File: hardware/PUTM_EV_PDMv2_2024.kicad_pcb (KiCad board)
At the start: 4 copper layers, 58 x 87.3 mm, 159 parts, among them IC1 BTS722204ESAXUMA1, IC2 BTS722204ESAXUMA1, IC3 BTS722204ESAXUMA1, IC4 BTS722204ESAXUMA1, J1 74650073R, J4 Conn_01x06, J5 UMPT-08-01-L-RA-WT-P-TR, J6 FTSH-107-01-L-DV-K-A, J7 USB_C_Receptacle_USB2.0_14P, J8 UMPT-08-01-L-RA-WT-P-TR, U1 STM32G0C1KCTxN, U2 LD1117S33TR_SOT223, U3 LM2675M-5.0/NOPB, U4 MCP2542FDxMF

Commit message: Changed CAN to isolated and added a new board-to-board plug
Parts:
- removed J4: Conn_01x06, Connector_IDC:IDC-Header_2x03_P2.54mm_Vertical
- removed J5, J8: UMPT-08-01-L-RA-WT-P-TR, UMPT-08-01-L-RA-WT-P-TR:SAMTEC_UMPT-08-01-L-RA-WT-P-TR
- removed the REF** at (174.6, 105.2)
- added C25: 100n, Capacitor_SMD:C_0603_1608Metric_Pad1.08x0.95mm_HandSolder, F.Cu at (211.2, 78.7)
- added C26: 10n, Capacitor_SMD:C_0603_1608Metric_Pad1.08x0.95mm_HandSolder, F.Cu at (211.2, 81.2)
- added C54: 47u, Capacitor_SMD:C_0603_1608Metric_Pad1.08x0.95mm_HandSolder, F.Cu at (211.2, 83.7)
- added C55: 220n, Capacitor_SMD:C_0603_1608Metric_Pad1.08x0.95mm_HandSolder, F.Cu at (211.2, 86.2)
- added C56: 100n, Capacitor_SMD:C_0603_1608Metric_Pad1.08x0.95mm_HandSolder, F.Cu at (211.2, 88.7)
- added C57: 47u, Capacitor_SMD:C_0603_1608Metric_Pad1.08x0.95mm_HandSolder, F.Cu at (211.2, 91.2)
- added C58: 100n, Capacitor_SMD:C_0603_1608Metric_Pad1.08x0.95mm_HandSolder, F.Cu at (211.2, 93.7)
- added C59: 10n, Capacitor_SMD:C_0603_1608Metric_Pad1.08x0.95mm_HandSolder, F.Cu at (211.2, 96.2)
- added D9: 5.3V/400W, Package_TO_SOT_SMD:SOT-23-3, F.Cu at (215.9, 94.1)
- added FB1: 2K@100MHz, Inductor_SMD:L_0805_2012Metric_Pad1.05x1.20mm_HandSolder, F.Cu at (228.7, 78.8)
- added FB2: 2K@100MHz, Inductor_SMD:L_0805_2012Metric_Pad1.05x1.20mm_HandSolder, F.Cu at (228.7, 81.5)
- added FB3: 2K@100MHz, Inductor_SMD:L_0805_2012Metric_Pad1.05x1.20mm_HandSolder, F.Cu at (228.7, 84.3)
- added FB4: 2K@100MHz, Inductor_SMD:L_0805_2012Metric_Pad1.05x1.20mm_HandSolder, F.Cu at (228.7, 87.0)
- added J2: IPBS-110-01-XX-D-GP, IPBS-110-01-T-D-GP:SAMTEC_IPBS-110-01-XX-D-GP, F.Cu at (199.1, 99.3)
- added R66: 100K, Resistor_SMD:R_0603_1608Metric_Pad0.98x0.95mm_HandSolder, F.Cu at (211.2, 98.8)
- added U4: ADM3057ExRW, Package_SO:SOIC-20W_7.5x12.8mm_P1.27mm, F.Cu at (219.8, 84.7)
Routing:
- net CAN_L: track 19.6 -> 10.1 mm
- net CAN_H: track 19.8 -> 10.5 mm
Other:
- board outline removed

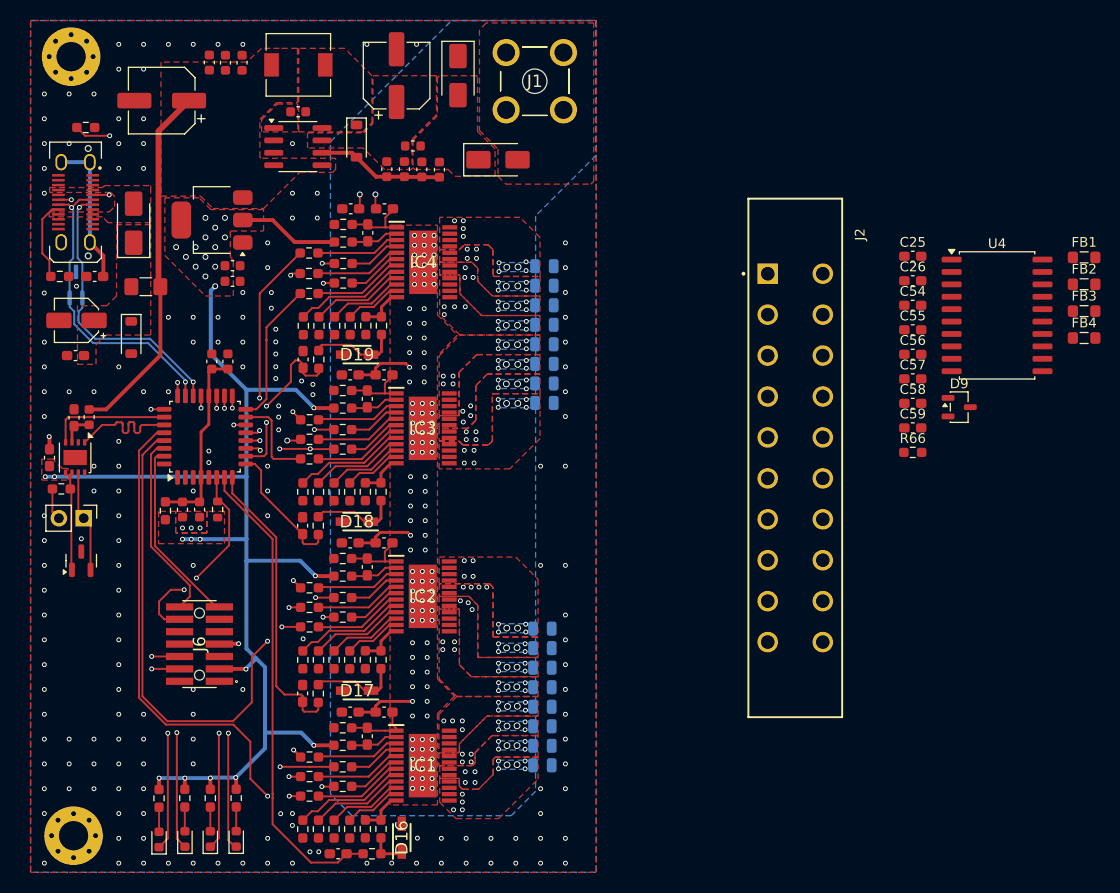
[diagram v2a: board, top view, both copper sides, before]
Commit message: new pcb layout & can coppied from steeringwheel
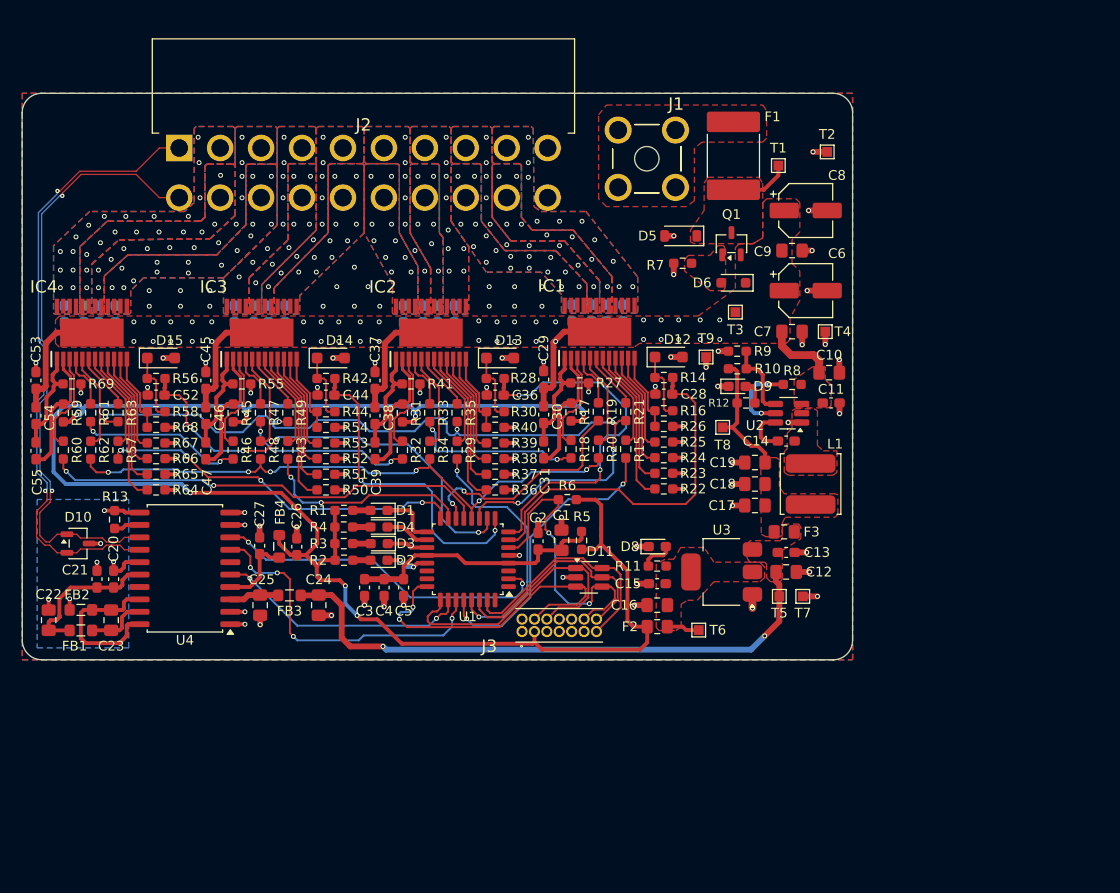
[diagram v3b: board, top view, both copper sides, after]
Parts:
- removed the C25 at (122.8, 99.3)
- removed the C25 at (211.2, 78.7)
- removed the C26 at (125.3, 95.2)
- removed the C26 at (211.2, 81.2)
- removed D16, D17, D18, D19: SKL34, SKL34:SODFL3718X140N
- removed the D9 at (215.9, 94.1)
- removed the D9 at (126.0, 109.8)
- removed the FB2 at (228.7, 81.5)
- removed the FB2 at (126.8, 95.2)
- removed G*** (x2): LOGO, LOGO
- removed G***: LOGO, Logos:SignatureBox25mm
- removed G***: LOGO, logos:PUTM_LOGO_15mm
- removed J6: FTSH-107-01-L-DV-K-A, FTSH-107-01-L-DV-K-A:FTSH-107-XX-YYY-DV-K-A
- removed J7: USB_C_Receptacle_USB2.0_14P, Connector_USB:USB_C_Receptacle_JAE_DX07S024WJ3R400
- removed JP1: Jumper_2_Bridged, Connector_PinHeader_2.54mm:PinHeader_1x02_P2.54mm_Vertical
- removed L2: 47u, Inductor_SMD:L_6.3x6.3_H3
- removed REF** (x2): MountingHole_3mm_Pad_Via, MountingHole:MountingHole_3mm_Pad_Via
- removed the U4 at (125.4, 99.3)
- removed the U4 at (219.8, 84.7)
- added C25: 47u, Capacitor_SMD:C_0805_2012Metric_Pad1.18x1.45mm_HandSolder, F.Cu at (144.3, 114.4)
- added C26: 100n, Capacitor_SMD:C_0603_1608Metric_Pad1.08x0.95mm_HandSolder, F.Cu at (148.1, 108.4)
- added D13: 40V/3A, Diode_SMD:D_SOD-123F, F.Cu at (168.9, 89.1)
- added D14: 40V/3A, Diode_SMD:D_SOD-123F, F.Cu at (151.6, 89.1)
- added D15: 40V/3A, Diode_SMD:D_SOD-123F, F.Cu at (134.2, 89.1)
- added D9: LED_+5V, LED_SMD:LED_0603_1608Metric_Pad1.05x0.95mm_HandSolder, F.Cu at (193.2, 92.0)
- added F2: 6V/1A, Fuse:Fuse_0805_2012Metric_Pad1.15x1.40mm_HandSolder, F.Cu at (185.0, 116.6)
- added F3: 6V/1A, Fuse:Fuse_0805_2012Metric_Pad1.15x1.40mm_HandSolder, F.Cu at (198.0, 106.9)
- added FB2: 2K@100MHz, Inductor_SMD:L_0805_2012Metric_Pad1.05x1.20mm_HandSolder, F.Cu at (126.0, 114.9)
- added J3: FTSH-107-01-L-D-K, PDM:FTSH-107-XX-YYY-D-K, F.Cu at (171.2, 117.1)
- added Q1: 30V/5A, Package_TO_SOT_SMD:SOT-23-3, F.Cu at (192.6, 77.4)
- added R67: 10k, Resistor_SMD:R_0603_1608Metric_Pad0.98x0.95mm_HandSolder, F.Cu at (133.7, 97.8)
- added R68: 1k2, Resistor_SMD:R_0603_1608Metric_Pad0.98x0.95mm_HandSolder, F.Cu at (133.7, 96.2)
- added R69: 47R, Resistor_SMD:R_0603_1608Metric_Pad0.98x0.95mm_HandSolder, F.Cu at (125.1, 91.8)
- added T1: TP_VCC, TestPoint:TestPoint_Pad_1.0x1.0mm, F.Cu at (197.4, 69.4)
- added T2: TP_GND, TestPoint:TestPoint_Pad_1.0x1.0mm, F.Cu at (202.4, 68.0)
- added T3: TP_VCC, TestPoint:TestPoint_Pad_1.0x1.0mm, F.Cu at (193.0, 84.4)
- added T4: TP_GND, TestPoint:TestPoint_Pad_1.0x1.0mm, F.Cu at (202.2, 86.4)
- added T5: TP_+5V, TestPoint:TestPoint_Pad_1.0x1.0mm, F.Cu at (197.5, 113.5)
- added T6: TP_+3V3, TestPoint:TestPoint_Pad_1.0x1.0mm, F.Cu at (189.2, 117.0)
- added T7: TP_GND, TestPoint:TestPoint_Pad_1.0x1.0mm, F.Cu at (199.9, 113.5)
- added T8: TP_+5V, TestPoint:TestPoint_Pad_1.0x1.0mm, F.Cu at (191.7, 96.2)
- added T9: TP_GND, TestPoint:TestPoint_Pad_1.0x1.0mm, F.Cu at (190.0, 89.0)
- added U4: ADM3057ExRW, Package_SO:SOIC-20W_7.5x12.8mm_P1.27mm, F.Cu at (136.7, 110.6)
- C1, C7: value 100n -> 10u; footprint Capacitor_SMD:C_0603_1608Metric -> Capacitor_SMD:C_0805_2012Metric_Pad1.18x1.45mm_HandSolder
- C10, C16: value 100n -> 22u; footprint Capacitor_SMD:C_0603_1608Metric -> Capacitor_SMD:C_0805_2012Metric_Pad1.18x1.45mm_HandSolder
- C11, C15, C5: value 1u -> 100n; footprint Capacitor_SMD:C_0603_1608Metric -> Capacitor_SMD:C_0603_1608Metric_Pad1.08x0.95mm_HandSolder
- C12: value 10n -> 10u; footprint Capacitor_SMD:C_0603_1608Metric -> Capacitor_SMD:C_0805_2012Metric_Pad1.18x1.45mm_HandSolder
- C13: footprint Capacitor_SMD:C_0603_1608Metric -> Capacitor_SMD:C_0603_1608Metric_Pad1.08x0.95mm_HandSolder
- C14: value 68u -> 100n; footprint Capacitor_SMD:CP_Elec_6.3x5.4 -> Capacitor_SMD:C_0603_1608Metric_Pad1.08x0.95mm_HandSolder
- C17: value 220p -> 22u; footprint Capacitor_SMD:C_0603_1608Metric_Pad1.08x0.95mm_HandSolder -> Capacitor_SMD:C_0805_2012Metric_Pad1.18x1.45mm_HandSolder
- C18: value 100n -> 22u; footprint Capacitor_SMD:C_0603_1608Metric_Pad1.08x0.95mm_HandSolder -> Capacitor_SMD:C_0805_2012Metric_Pad1.18x1.45mm_HandSolder
- C19: value 22n -> 22u; footprint Capacitor_SMD:C_0603_1608Metric_Pad1.08x0.95mm_HandSolder -> Capacitor_SMD:C_0805_2012Metric_Pad1.18x1.45mm_HandSolder
- C2: value 4.7u -> 4u7; footprint Capacitor_SMD:C_0603_1608Metric -> Capacitor_SMD:C_0603_1608Metric_Pad1.08x0.95mm_HandSolder
- C20: value 470n -> 100n
- C21: footprint Capacitor_SMD:C_0805_2012Metric -> Capacitor_SMD:C_0603_1608Metric_Pad1.08x0.95mm_HandSolder; moved to F.Cu
- C22, C23, C24: value 10n -> 47u; footprint Capacitor_SMD:C_0805_2012Metric -> Capacitor_SMD:C_0805_2012Metric_Pad1.18x1.45mm_HandSolder; moved to F.Cu
- C27: value 22u -> 10n; footprint Capacitor_SMD:CP_Elec_4x4.5 -> Capacitor_SMD:C_0603_1608Metric_Pad1.08x0.95mm_HandSolder
- C28: value 1u -> 220p
- C29, C37, C45: value 220p -> 100n
- C3: value 100n -> 4u7; footprint Capacitor_SMD:C_0603_1608Metric -> Capacitor_SMD:C_0603_1608Metric_Pad1.08x0.95mm_HandSolder
- C30, C38, C46: value 100n -> 22n
- C31, C39, C47: value 22n -> 470n
- C32, C40, C48: value 470n -> 10n; moved to B.Cu
- C33, C34, C35, C41, C42, C43, C49, C50, C51: footprint Capacitor_SMD:C_0805_2012Metric -> Capacitor_SMD:C_0603_1608Metric_Pad1.08x0.95mm_HandSolder
- C36, C44, C52: value 10n -> 220p; footprint Capacitor_SMD:C_0805_2012Metric -> Capacitor_SMD:C_0603_1608Metric_Pad1.08x0.95mm_HandSolder; moved to F.Cu
- C4: value 4.7u -> 100n; footprint Capacitor_SMD:C_0603_1608Metric -> Capacitor_SMD:C_0603_1608Metric_Pad1.08x0.95mm_HandSolder
- C53: value 10n -> 100n
- C54: value 47u -> 22n
- C55: value 220n -> 470n
- C56, C58: value 100n -> 10n; moved to B.Cu
- C57: value 47u -> 10n; moved to B.Cu
- C59: moved to B.Cu
- C6: value 10u -> 22u; footprint Capacitor_SMD:C_0603_1608Metric -> Capacitor_SMD:CP_Elec_5x5.8
- C8: value 100n -> 22u; footprint Capacitor_SMD:C_0603_1608Metric -> Capacitor_SMD:CP_Elec_5x5.8
- C9: value 100u -> 10u; footprint Capacitor_SMD:CP_Elec_6.3x7.7 -> Capacitor_SMD:C_0805_2012Metric_Pad1.18x1.45mm_HandSolder
- D1, D2, D3, D4: value 150060SS75000 -> LED_Debug; footprint LED_SMD:LED_0603_1608Metric -> LED_SMD:LED_0603_1608Metric_Pad1.05x0.95mm_HandSolder
- D10: value 0.1/1A -> PESD5V0L2BT,215; footprint Diode_SMD:D_SMA -> Package_TO_SOT_SMD:SOT-23-3
- D11: value 6V -> SP0505BAHTG; footprint Diode_SMD:D_SOD-123 -> Package_TO_SOT_SMD:SOT-23-6_Handsoldering
- D12: value TPD2E2U06QDCKRQ1 -> 40V/3A; footprint Package_TO_SOT_SMD:SOT-323_SC-70_Handsoldering -> Diode_SMD:D_SOD-123F; moved to F.Cu
- D5: value SMAJ24CA-13-F -> 30V/200W; footprint Diode_SMD:D_SMA -> Diode_SMD:D_SOD-123
- D6: value SS26FL -> 9V1/200mW; footprint Diode_SMD:D_SOD-123 -> Diode_SMD:D_SOD-323_HandSoldering
- D8: value SS34ALH -> LED_+3V3; footprint Diode_SMD:D_SMA -> LED_SMD:LED_0603_1608Metric_Pad1.05x0.95mm_HandSolder
- F1: value 5V/0.5A -> 33V/1A5; footprint Fuse:Fuse_1206_3216Metric_Pad1.42x1.75mm_HandSolder -> Fuse:Fuse_2920_7451Metric_Pad2.10x5.45mm_HandSolder
- IC1, IC2, IC3, IC4: footprint BTS722204ESAXUMA1:SOP65P600X115-25N -> PDM:SOP65P600X115-25N
- J1: footprint Redcube conn:74650073R -> PDM:74650073R
- J2: footprint IPBS-110-01-T-D-GP:SAMTEC_IPBS-110-01-XX-D-GP -> PDM:IPBT110H1TDRAGP
- L1: value 300n -> 68u/1A4; footprint Inductor_SMD:L_0603_1608Metric -> Inductor_SMD:L_TDK_VLS6045EX_VLS6045AF
- R1, R2, R3, R4: value 150 -> 150R
- R10: value 10k -> 100k
- R11, R12: value 10k -> 1k
- R13: value 1.2k -> 100k
- R14: value 47 -> 4k7
- R15, R16: value 330 -> 4k7
- R17: value 330 -> 470R
- R18, R34, R35, R48, R49, R62, R63: value 330 -> 330R
- R19: value 100k -> 330R; footprint Resistor_SMD:R_0603_1608Metric -> Resistor_SMD:R_0603_1608Metric_Pad0.98x0.95mm_HandSolder
- R20: value 0 -> 330R
- R21: value 120 -> 330R
- R22, R23: value 5.1k -> 10k
- R24, R25, R38, R39, R52, R53: value 4.7k -> 10k
- R26, R40, R54: value 470 -> 1k2
- R27, R41, R55: value 4.7k -> 47R
- R28, R29, R30, R42, R43, R44, R56, R57, R58: value 10k -> 4k7
- R31, R45, R59: value 10k -> 470R
- R32, R46, R60: value 1.2k -> 330R
- R33, R47, R61: value 47 -> 330R
- R36, R37, R50, R51, R64, R65: value 330 -> 10k
- R5: value 4.7k -> 0
- R6: value 4.7k -> 100k
- R66: value 100K -> 10k
- R7: value 470 -> 100k
- R8: value 4.7k -> 510k
- R9: value 10k -> 13k3
- U2: value LD1117S33TR_SOT223 -> TPS54202HDDCR; footprint Package_TO_SOT_SMD:SOT-223-3_TabPin2 -> Package_TO_SOT_SMD:SOT-23-6_Handsoldering
- U3: value LM2675M-5.0/NOPB -> LM1117-3.3; footprint Package_SO:SOIC-8_3.9x4.9mm_P1.27mm -> Package_TO_SOT_SMD:SOT-223-3_TabPin2
- moved FB1 109.6 mm to (126.0, 117.0)
- moved C55 90.6 mm to (121.4, 98.6), turned to -90 degrees
- moved C54 90.5 mm to (121.4, 95.0), turned to -90 degrees
- moved C56 86.9 mm to (124.3, 84.6), turned to -90 degrees
- moved FB3 86.4 mm to (147.3, 113.4)
- moved FB4 85.1 mm to (146.3, 108.4), turned to 90 degrees
- moved C57 85.1 mm to (126.3, 84.6), turned to -90 degrees
- moved C58 83.8 mm to (127.8, 84.6), turned to -90 degrees
- moved C59 82.5 mm to (129.5, 84.6), turned to -90 degrees
- moved R66 77.5 mm to (133.7, 99.4), turned to 180 degrees
- moved C14 72.8 mm to (198.2, 97.6), turned to 0 degrees
- moved C16 72.0 mm to (185.0, 114.4), turned to 180 degrees
- moved J2 70.6 mm to (136.1, 67.6), turned to 0 degrees
- moved R22 69.8 mm to (185.7, 102.5)
- moved C10 69.5 mm to (202.6, 90.6), turned to 0 degrees
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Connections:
- C1 pad 1: /STM_VCC -> /MCU/STM_VCC
- C10 pad 1: +5V -> +24V
- C11 pad 1: +3.3V -> GND
- C11 pad 2: GND -> +24V
- C12 pad 1: /Power/CB -> +5V
- C12 pad 2: /Power/SW_L -> GND
- C13 pad 1: +3.3V -> +5V
- C14 pad 1: +5V -> /Power/BOOT_+5V
- C14 pad 2: GND -> /Power/SW_+5V
- C15 pad 1: +5V -> /Power/VO_+3.3V
- C16 pad 1: +5V -> /Power/VO_+3.3V
- C17 pad 1: /FUSE1_IS -> /Power/+5V_OUT
- C18 pad 1: +BATT -> /Power/+5V_OUT
- C19 pad 1: +BATT -> /Power/+5V_OUT
- C19 pad 2: Net-(IC1-GND_1) -> GND
- C2 pad 1: /STM_VCC -> /MCU/STM_VCC
- C20 pad 1: Net-(IC1-GND_1) -> /CAN/CAN_GND_ISO
- C20 pad 2: Net-(IC1-VDD) -> /CAN/VISOIN
- C21 pad 1: OUT1_0 -> /CAN/VISOIN
- C21 pad 2: GND -> /CAN/CAN_GND_ISO
- C22 pad 1: OUT1_1 -> /CAN/CAN_GND_ISO
- C22 pad 2: GND -> /CAN/VISOIN
- C23 pad 1: OUT1_2 -> /CAN/GNDISO
- C23 pad 2: GND -> /CAN/VISOOUT
- C24 pad 1: OUT1_3 -> GND
- C24 pad 2: GND -> +5V
- C27 pad 1: Net-(D10-K) -> /CAN/VIO
- C28 pad 1: Net-(D10-K) -> /MCU/FUSE_IS0
- C29 pad 1: /FUSE2_IS -> +24V
- C3 pad 1: /STM_VCC -> /MCU/STM_VCC
- C30 pad 1: +BATT -> +24V
- C30 pad 2: GND -> /Power controllers/IC_0/PC0_GND
- C31 pad 1: +BATT -> /Power controllers/IC_0/PC0_GND
- C31 pad 2: Net-(IC2-GND_1) -> /Power controllers/IC_0/VDD
- C32 pad 1: Net-(IC2-GND_1) -> OUT0_0
- C32 pad 2: Net-(IC2-VDD) -> GND
- C33 pad 1: OUT2_0 -> OUT0_1
- C34 pad 1: OUT2_1 -> OUT0_2
- C35 pad 1: OUT2_2 -> OUT0_3
- C36 pad 1: OUT2_3 -> /MCU/FUSE_IS1
- C37 pad 1: /FUSE3_IS -> +24V
- C38 pad 1: +BATT -> +24V
- C38 pad 2: GND -> /Power controllers/IC_1/PC1_GND
- C39 pad 1: +BATT -> /Power controllers/IC_1/PC1_GND
- C39 pad 2: Net-(IC3-GND_1) -> /Power controllers/IC_1/VDD
- C4 pad 1: /STM_VCC -> /MCU/STM_VCC
- C40 pad 1: Net-(IC3-GND_1) -> OUT1_0
- C40 pad 2: Net-(IC3-VDD) -> GND
- C41 pad 1: OUT3_0 -> OUT1_1
- C42 pad 1: OUT3_1 -> OUT1_2
- C43 pad 1: OUT3_2 -> OUT1_3
- C44 pad 1: OUT3_3 -> /MCU/FUSE_IS2
- C45 pad 1: /FUSE4_IS -> +24V
- C46 pad 1: +BATT -> +24V
- C46 pad 2: GND -> /Power controllers/IC_2/PC2_GND
- C47 pad 1: +BATT -> /Power controllers/IC_2/PC2_GND
- C47 pad 2: Net-(IC4-GND_1) -> /Power controllers/IC_2/VDD
- C48 pad 1: Net-(IC4-GND_1) -> OUT2_0
- C48 pad 2: Net-(IC4-VDD) -> GND
- C49 pad 1: OUT4_0 -> OUT2_1
- C5 pad 1: GND -> /MCU/STM_VCC
- C5 pad 2: /Power/VIN_L -> GND
- C50 pad 1: OUT4_1 -> OUT2_2
- C51 pad 1: OUT4_2 -> OUT2_3
- C52 pad 1: OUT4_3 -> /MCU/FUSE_IS3
- C53 pad 1: Net-(J7-SHIELD) -> +24V
- C54 pad 1: /CAN/GNDISO_CAN -> +24V
- C54 pad 2: Net-(U4-VISOIN) -> /Power controllers/IC_3/PC3_GND
- C55 pad 1: Net-(C55-Pad1) -> /Power controllers/IC_3/PC3_GND
- C55 pad 2: Net-(U4-VISOOUT) -> /Power controllers/IC_3/VDD
- C56 pad 1: GND -> OUT3_0
- C56 pad 2: +5V -> GND
- C57 pad 1: GND -> OUT3_1
- C57 pad 2: Net-(U4-VCC) -> GND
- C58 pad 1: +3.3V -> OUT3_2
- C59 pad 1: Net-(U4-VIO) -> OUT3_3
- C6 pad 1: GND -> +24V
- C6 pad 2: /Power/VIN_L -> GND
- C7 pad 1: GND -> +24V
- C7 pad 2: /Power/VIN_SW_REG -> GND
- C8 pad 1: GND -> +24V
- C8 pad 2: /Power/VIN_SW_REG -> GND
- C9 pad 1: /Power/VIN_SW_REG -> +24V
- D1 pad 1: /LED1 -> /MCU/LED3
- D1 pad 2: Net-(D1-A) -> /MCU/LD_3_R
- D10 pad 1: Net-(D10-K) -> /CAN/CAN.N
- D10 pad 2: VBUS -> /CAN/CAN.P
- D11 pad 1: Net-(D10-K) -> /Connectors/SW.CLK
- D12 pad 1: /D- -> /Power controllers/IC_0/R_IS_PROT
- D12 pad 2: /D+ -> GND
- D2 pad 1: /LED2 -> /MCU/LED2
- D2 pad 2: Net-(D2-A) -> /MCU/LD_2_R
- D3 pad 1: /LED3 -> /MCU/LED1
- D3 pad 2: Net-(D3-A) -> /MCU/LD_1_R
- D4 pad 1: /LED4 -> /MCU/LED0
- D4 pad 2: Net-(D4-A) -> /MCU/LD_0_R
- D5 pad 1: GND -> /Power/RPP_D
- D5 pad 2: /Power/VIN_L -> GND
- D6 pad 1: /Power/SW_L -> +24V
- D6 pad 2: GND -> /Power/RPP_G
- D8 pad 1: /Power/VIN_L -> GND
- D8 pad 2: +BATT -> /Power/D3V3_R1k
- F1 pad 1: +5V -> /Power/RPP_D
- F1 pad 2: Net-(D10-K) -> +BATT
- FB1 pad 1: Net-(U4-VISOIN) -> /CAN/VISOIN
- FB1 pad 2: Net-(U4-VISOOUT) -> /CAN/VISOOUT
- FB3 pad 1: Net-(U4-VCC) -> /CAN/VCC
- FB4 pad 1: Net-(U4-VIO) -> /CAN/VIO
- FB4 pad 2: +3.3V -> +3V3
- IC1 pad 1: Net-(IC1-GND_1) -> /Power controllers/IC_0/PC0_GND
- IC1 pad 10: /Controllers/IC_1/IN2 -> /Power controllers/IC_0/IN2
- IC1 pad 11: /Controllers/IC_1/IN3 -> /Power controllers/IC_0/IN3
- IC1 pad 12: Net-(IC1-IS) -> /Power controllers/IC_0/IS
- IC1 pad 13: OUT1_3 -> OUT0_3
- IC1 pad 14: OUT1_3 -> OUT0_3
- IC1 pad 15: OUT1_3 -> OUT0_3
- IC1 pad 16: OUT1_3 -> OUT0_3
- IC1 pad 17: OUT1_2 -> OUT0_2
- IC1 pad 18: OUT1_2 -> OUT0_2
- IC1 pad 19: OUT1_1 -> OUT0_1
- IC1 pad 2: Net-(IC1-VDD) -> /Power controllers/IC_0/VDD
- IC1 pad 20: OUT1_1 -> OUT0_1
- IC1 pad 21: OUT1_0 -> OUT0_0
- IC1 pad 22: OUT1_0 -> OUT0_0
- IC1 pad 23: OUT1_0 -> OUT0_0
- IC1 pad 24: OUT1_0 -> OUT0_0
- IC1 pad 25: +BATT -> +24V
- IC1 pad 3: Net-(IC1-SO) -> /Power controllers/IC_0/SO
- IC1 pad 4: Net-(IC1-SI) -> /Power controllers/IC_0/SI
- IC1 pad 5: Net-(IC1-SCLK) -> /Power controllers/IC_0/SCLK
- IC1 pad 6: Net-(IC1-CSN) -> /Power controllers/IC_0/CSN
- IC1 pad 7: Net-(IC1-LHI) -> /Power controllers/IC_0/LHI
- IC1 pad 8: /Controllers/IC_1/IN0 -> /Power controllers/IC_0/IN0
- IC1 pad 9: /Controllers/IC_1/IN1 -> /Power controllers/IC_0/IN1
- IC2 pad 1: Net-(IC2-GND_1) -> /Power controllers/IC_1/PC1_GND
- IC2 pad 10: /Controllers/IC_2/IN2 -> /Power controllers/IC_1/IN2
- IC2 pad 11: /Controllers/IC_2/IN3 -> /Power controllers/IC_1/IN3
- IC2 pad 12: Net-(IC2-IS) -> /Power controllers/IC_1/IS
- IC2 pad 13: OUT2_3 -> OUT1_3
- IC2 pad 14: OUT2_3 -> OUT1_3
- IC2 pad 15: OUT2_3 -> OUT1_3
- IC2 pad 16: OUT2_3 -> OUT1_3
- IC2 pad 17: OUT2_2 -> OUT1_2
- IC2 pad 18: OUT2_2 -> OUT1_2
- IC2 pad 19: OUT2_1 -> OUT1_1
- IC2 pad 2: Net-(IC2-VDD) -> /Power controllers/IC_1/VDD
- IC2 pad 20: OUT2_1 -> OUT1_1
- IC2 pad 21: OUT2_0 -> OUT1_0
- IC2 pad 22: OUT2_0 -> OUT1_0
- IC2 pad 23: OUT2_0 -> OUT1_0
- IC2 pad 24: OUT2_0 -> OUT1_0
- IC2 pad 25: +BATT -> +24V
- IC2 pad 3: Net-(IC2-SO) -> /Power controllers/IC_1/SO
- IC2 pad 4: Net-(IC2-SI) -> /Power controllers/IC_1/SI
- IC2 pad 5: Net-(IC2-SCLK) -> /Power controllers/IC_1/SCLK
- IC2 pad 6: Net-(IC2-CSN) -> /Power controllers/IC_1/CSN
- IC2 pad 7: Net-(IC2-LHI) -> /Power controllers/IC_1/LHI
- IC2 pad 8: /Controllers/IC_2/IN0 -> /Power controllers/IC_1/IN0
- IC2 pad 9: /Controllers/IC_2/IN1 -> /Power controllers/IC_1/IN1
- IC3 pad 1: Net-(IC3-GND_1) -> /Power controllers/IC_2/PC2_GND
- IC3 pad 10: /Controllers/IC_3/IN2 -> /Power controllers/IC_2/IN2
- IC3 pad 11: /Controllers/IC_3/IN3 -> /Power controllers/IC_2/IN3
- IC3 pad 12: Net-(IC3-IS) -> /Power controllers/IC_2/IS
- IC3 pad 13: OUT3_3 -> OUT2_3
- IC3 pad 14: OUT3_3 -> OUT2_3
- IC3 pad 15: OUT3_3 -> OUT2_3
- IC3 pad 16: OUT3_3 -> OUT2_3
- IC3 pad 17: OUT3_2 -> OUT2_2
- IC3 pad 18: OUT3_2 -> OUT2_2
- IC3 pad 19: OUT3_1 -> OUT2_1
- IC3 pad 2: Net-(IC3-VDD) -> /Power controllers/IC_2/VDD
- IC3 pad 20: OUT3_1 -> OUT2_1
- IC3 pad 21: OUT3_0 -> OUT2_0
- IC3 pad 22: OUT3_0 -> OUT2_0
- IC3 pad 23: OUT3_0 -> OUT2_0
- IC3 pad 24: OUT3_0 -> OUT2_0
- IC3 pad 25: +BATT -> +24V
- IC3 pad 3: Net-(IC3-SO) -> /Power controllers/IC_2/SO
- IC3 pad 4: Net-(IC3-SI) -> /Power controllers/IC_2/SI
- IC3 pad 5: Net-(IC3-SCLK) -> /Power controllers/IC_2/SCLK
- IC3 pad 6: Net-(IC3-CSN) -> /Power controllers/IC_2/CSN
- IC3 pad 7: Net-(IC3-LHI) -> /Power controllers/IC_2/LHI
- IC3 pad 8: /Controllers/IC_3/IN0 -> /Power controllers/IC_2/IN0
- IC3 pad 9: /Controllers/IC_3/IN1 -> /Power controllers/IC_2/IN1
- IC4 pad 1: Net-(IC4-GND_1) -> /Power controllers/IC_3/PC3_GND
- IC4 pad 10: /Controllers/IC_4/IN2 -> /Power controllers/IC_3/IN2
- IC4 pad 11: /Controllers/IC_4/IN3 -> /Power controllers/IC_3/IN3
- IC4 pad 12: Net-(IC4-IS) -> /Power controllers/IC_3/IS
- IC4 pad 13: OUT4_3 -> OUT3_3
- IC4 pad 14: OUT4_3 -> OUT3_3
- IC4 pad 15: OUT4_3 -> OUT3_3
- IC4 pad 16: OUT4_3 -> OUT3_3
- IC4 pad 17: OUT4_2 -> OUT3_2
- IC4 pad 18: OUT4_2 -> OUT3_2
- IC4 pad 19: OUT4_1 -> OUT3_1
- IC4 pad 2: Net-(IC4-VDD) -> /Power controllers/IC_3/VDD
- IC4 pad 20: OUT4_1 -> OUT3_1
- IC4 pad 21: OUT4_0 -> OUT3_0
- IC4 pad 22: OUT4_0 -> OUT3_0
- IC4 pad 23: OUT4_0 -> OUT3_0
- IC4 pad 24: OUT4_0 -> OUT3_0
- IC4 pad 25: +BATT -> +24V
- IC4 pad 3: Net-(IC4-SO) -> /Power controllers/IC_3/SO
- IC4 pad 4: Net-(IC4-SI) -> /Power controllers/IC_3/SI
- IC4 pad 5: Net-(IC4-SCLK) -> /Power controllers/IC_3/SCLK
- IC4 pad 6: Net-(IC4-CSN) -> /Power controllers/IC_3/CSN
- IC4 pad 7: Net-(IC4-LHI) -> /Power controllers/IC_3/LHI
- IC4 pad 8: /Controllers/IC_4/IN0 -> /Power controllers/IC_3/IN0
- IC4 pad 9: /Controllers/IC_4/IN1 -> /Power controllers/IC_3/IN1
- J2 pad 10: OUT2_1 -> unconnected-(J2-Pad10)
- J2 pad 11: CAN_L -> /CAN/CAN.N
- J2 pad 12: CAN_H -> OUT3_1
- J2 pad 13: ASMS -> OUT3_3
- J2 pad 14: unconnected-(J2-Pad14) -> OUT2_1
- J2 pad 15: OUT1_3 -> OUT2_3
- J2 pad 16: OUT1_2 -> OUT1_0
- J2 pad 17: OUT1_1 -> OUT1_2
- J2 pad 18: OUT1_0 -> OUT0_0
- J2 pad 19: OUT2_3 -> OUT0_2
- J2 pad 20: OUT2_2 -> GND
- L1 pad 1: /Power/VIN_L -> /Power/SW_+5V
- L1 pad 2: /Power/VIN_SW_REG -> /Power/+5V_OUT
- R1 pad 1: +3.3V -> /MCU/LD_3_R
- R1 pad 2: Net-(D3-A) -> +3V3
- R10 pad 1: GND -> /Power/FB_+5V
- R10 pad 2: /Controllers/IC_1/IN1 -> /Power/+5V_OUT
- R11 pad 1: GND -> /Power/VO_+3.3V
- R11 pad 2: /Controllers/IC_1/IN2 -> /Power/D3V3_R1k
- R12 pad 1: GND -> /Power/+5V_OUT
- R12 pad 2: /Controllers/IC_1/IN3 -> /Power/D5V_R1k
- R13 pad 1: Net-(IC1-IS) -> /CAN/CAN_GND_ISO
- R13 pad 2: GND -> /CAN/RS
- R14 pad 1: GND -> /MCU/FUSE_IS0
- R14 pad 2: Net-(IC1-GND_1) -> /Power controllers/IC_0/R_IS_PROT
- R15 pad 1: /Controllers/MISO_1 -> /MCU/LHI0
- R15 pad 2: Net-(IC1-SO) -> /Power controllers/IC_0/LHI
- R16 pad 1: /SPI1_MOSI -> /Power controllers/IC_0/R_IS_PROT
- R16 pad 2: Net-(IC1-SI) -> /Power controllers/IC_0/IS
- R17 pad 1: /SPI1_SCK -> +3V3
- R17 pad 2: Net-(IC1-SCLK) -> /Power controllers/IC_0/VDD
- R18 pad 1: /SPI1_NSS -> /Power controllers/IC_0/MISO
- R18 pad 2: Net-(IC1-CSN) -> /Power controllers/IC_0/SO
- R19 pad 1: +3.3V -> /MCU/SPI.MOSI
- R19 pad 2: /NRST -> /Power controllers/IC_0/SI
- R2 pad 1: +3.3V -> /MCU/LD_2_R
- R2 pad 2: Net-(D2-A) -> +3V3
- R20 pad 1: +3.3V -> /MCU/SPI.SCK
- R20 pad 2: /STM_VCC -> /Power controllers/IC_0/SCLK
- R21 pad 1: Net-(JP1-B) -> /MCU/SPI.NSS
- R21 pad 2: CAN_L -> /Power controllers/IC_0/CSN
- R22 pad 2: Net-(J7-CC1) -> /Power controllers/IC_0/IN0
- R23 pad 2: Net-(J7-CC2) -> /Power controllers/IC_0/IN1
- R24 pad 1: /FUSE2_IS -> GND
- R24 pad 2: Net-(D17-K) -> /Power controllers/IC_0/IN2
- R25 pad 1: /LHI_2 -> GND
- R25 pad 2: Net-(IC2-LHI) -> /Power controllers/IC_0/IN3
- R26 pad 1: +3.3V -> /Power controllers/IC_0/IS
- R26 pad 2: Net-(IC2-VDD) -> GND
- R27 pad 1: Net-(D17-K) -> GND
- R27 pad 2: Net-(IC2-IS) -> /Power controllers/IC_0/PC0_GND
- R28 pad 1: GND -> /MCU/FUSE_IS1
- R28 pad 2: /Controllers/IC_2/IN0 -> /Power controllers/IC_1/R_IS_PROT
- R29 pad 1: GND -> /MCU/LHI1
- R29 pad 2: /Controllers/IC_2/IN1 -> /Power controllers/IC_1/LHI
- R3 pad 1: +3.3V -> /MCU/LD_1_R
- R3 pad 2: Net-(D1-A) -> +3V3
- R30 pad 1: GND -> /Power controllers/IC_1/R_IS_PROT
- R30 pad 2: /Controllers/IC_2/IN2 -> /Power controllers/IC_1/IS
- R31 pad 1: GND -> +3V3
- R31 pad 2: /Controllers/IC_2/IN3 -> /Power controllers/IC_1/VDD
- R32 pad 1: Net-(IC2-IS) -> /Power controllers/IC_1/MISO
- R32 pad 2: GND -> /Power controllers/IC_1/SO
- R33 pad 1: GND -> /Power controllers/IC_0/MISO
- R33 pad 2: Net-(IC2-GND_1) -> /Power controllers/IC_1/SI
- R34 pad 1: /Controllers/MISO_2 -> /MCU/SPI.SCK
- R34 pad 2: Net-(IC2-SO) -> /Power controllers/IC_1/SCLK
- R35 pad 1: /Controllers/MISO_1 -> /MCU/SPI.NSS
- R35 pad 2: Net-(IC2-SI) -> /Power controllers/IC_1/CSN
- R36 pad 1: /SPI1_SCK -> GND
- R36 pad 2: Net-(IC2-SCLK) -> /Power controllers/IC_1/IN0
- R37 pad 1: /SPI1_NSS -> GND
- R37 pad 2: Net-(IC2-CSN) -> /Power controllers/IC_1/IN1
- R38 pad 1: /FUSE3_IS -> GND
- R38 pad 2: Net-(D18-K) -> /Power controllers/IC_1/IN2
- R39 pad 1: /LHI_3 -> GND
- R39 pad 2: Net-(IC3-LHI) -> /Power controllers/IC_1/IN3
- R4 pad 1: +3.3V -> /MCU/LD_0_R
- R4 pad 2: Net-(D4-A) -> +3V3
- R40 pad 1: +3.3V -> /Power controllers/IC_1/IS
- R40 pad 2: Net-(IC3-VDD) -> GND
- R41 pad 1: Net-(D18-K) -> GND
- R41 pad 2: Net-(IC3-IS) -> /Power controllers/IC_1/PC1_GND
- R42 pad 1: GND -> /MCU/FUSE_IS2
- R42 pad 2: /Controllers/IC_3/IN0 -> /Power controllers/IC_2/R_IS_PROT
- R43 pad 1: GND -> /MCU/LHI2
- R43 pad 2: /Controllers/IC_3/IN1 -> /Power controllers/IC_2/LHI
- R44 pad 1: GND -> /Power controllers/IC_2/R_IS_PROT
- R44 pad 2: /Controllers/IC_3/IN2 -> /Power controllers/IC_2/IS
- R45 pad 1: GND -> +3V3
- R45 pad 2: /Controllers/IC_3/IN3 -> /Power controllers/IC_2/VDD
- R46 pad 1: Net-(IC3-IS) -> /Power controllers/IC_2/MISO
- R46 pad 2: GND -> /Power controllers/IC_2/SO
- R47 pad 1: GND -> /Power controllers/IC_1/MISO
- R47 pad 2: Net-(IC3-GND_1) -> /Power controllers/IC_2/SI
- R48 pad 1: /Controllers/MISO_3 -> /MCU/SPI.SCK
- R48 pad 2: Net-(IC3-SO) -> /Power controllers/IC_2/SCLK
- R49 pad 1: /Controllers/MISO_2 -> /MCU/SPI.NSS
- R49 pad 2: Net-(IC3-SI) -> /Power controllers/IC_2/CSN
- R5 pad 1: /FUSE1_IS -> +3V3
- R5 pad 2: Net-(D16-K) -> /MCU/STM_VCC
- R50 pad 1: /SPI1_SCK -> GND
- R50 pad 2: Net-(IC3-SCLK) -> /Power controllers/IC_2/IN0
- R51 pad 1: /SPI1_NSS -> GND
- R51 pad 2: Net-(IC3-CSN) -> /Power controllers/IC_2/IN1
- R52 pad 1: /FUSE4_IS -> GND
- R52 pad 2: Net-(D19-K) -> /Power controllers/IC_2/IN2
- R53 pad 1: /LHI_4 -> GND
- R53 pad 2: Net-(IC4-LHI) -> /Power controllers/IC_2/IN3
- R54 pad 1: +3.3V -> /Power controllers/IC_2/IS
- R54 pad 2: Net-(IC4-VDD) -> GND
- R55 pad 1: Net-(D19-K) -> GND
- R55 pad 2: Net-(IC4-IS) -> /Power controllers/IC_2/PC2_GND
- R56 pad 1: GND -> /MCU/FUSE_IS3
- R56 pad 2: /Controllers/IC_4/IN0 -> /Power controllers/IC_3/R_IS_PROT
- R57 pad 1: GND -> /MCU/LHI3
- R57 pad 2: /Controllers/IC_4/IN1 -> /Power controllers/IC_3/LHI
- R58 pad 1: GND -> /Power controllers/IC_3/R_IS_PROT
- R58 pad 2: /Controllers/IC_4/IN2 -> /Power controllers/IC_3/IS
- R59 pad 1: GND -> +3V3
- R59 pad 2: /Controllers/IC_4/IN3 -> /Power controllers/IC_3/VDD
- R6 pad 1: /LHI_1 -> +3V3
- R6 pad 2: Net-(IC1-LHI) -> /Connectors/RST
- R60 pad 1: Net-(IC4-IS) -> /MCU/SPI.MISO
- R60 pad 2: GND -> /Power controllers/IC_3/SO
- R61 pad 1: GND -> /Power controllers/IC_2/MISO
- R61 pad 2: Net-(IC4-GND_1) -> /Power controllers/IC_3/SI
- R62 pad 1: /SPI1_MISO -> /MCU/SPI.SCK
- R62 pad 2: Net-(IC4-SO) -> /Power controllers/IC_3/SCLK
- R63 pad 1: /Controllers/MISO_3 -> /MCU/SPI.NSS
- R63 pad 2: Net-(IC4-SI) -> /Power controllers/IC_3/CSN
- R64 pad 1: /SPI1_SCK -> GND
- R64 pad 2: Net-(IC4-SCLK) -> /Power controllers/IC_3/IN0
- R65 pad 1: /SPI1_NSS -> GND
- R65 pad 2: Net-(IC4-CSN) -> /Power controllers/IC_3/IN1
- R66 pad 1: /CAN/GNDISO_CAN -> GND
- R66 pad 2: Net-(U4-RS) -> /Power controllers/IC_3/IN2
- R7 pad 1: +3.3V -> GND
- R7 pad 2: Net-(IC1-VDD) -> /Power/RPP_G
- R8 pad 1: Net-(D16-K) -> /Power/EN
- R8 pad 2: Net-(IC1-IS) -> +24V
- R9 pad 2: /Controllers/IC_1/IN0 -> /Power/FB_+5V
- U1 pad 10: /FUSE4_IS -> /MCU/FUSE_IS3
- U1 pad 11: /SPI1_NSS -> /MCU/SPI.NSS
- U1 pad 12: /SPI1_SCK -> /MCU/SPI.SCK
- U1 pad 13: /SPI1_MISO -> /MCU/SPI.MISO
- U1 pad 14: /SPI1_MOSI -> /MCU/SPI.MOSI
- U1 pad 15: /LHI_3 -> /MCU/LHI2
- U1 pad 16: /LHI_4 -> /MCU/LHI3
- U1 pad 17: /LED4 -> /MCU/LED3
- U1 pad 18: /LED3 -> /MCU/LED0
- U1 pad 19: /LED2 -> /MCU/LED1
- U1 pad 2: unconnected-(U1-PC14-Pad2) -> /CAN/STBY_CAN
- U1 pad 20: /STM_VCC -> /MCU/STM_VCC
- U1 pad 21: /LED1 -> /MCU/LED2
- U1 pad 22: /D- -> unconnected-(U1-PA11/PA9-Pad22)
- U1 pad 23: /D+ -> unconnected-(U1-PA12/PA10-Pad23)
- U1 pad 24: /SWDIO -> /Connectors/SW.DIO
- U1 pad 25: /SWCLK -> /Connectors/SW.CLK
- U1 pad 26: /CAN_RXD -> /CAN/CAN.RX
- U1 pad 27: /CAN_TXD -> /CAN/CAN.TX
- U1 pad 28: /LHI_1 -> /MCU/LHI0
- U1 pad 29: /LHI_2 -> /MCU/LHI1
- U1 pad 30: /USART1_TX -> /Connectors/USART.TX
- U1 pad 31: /USART1_RX -> /Connectors/USART.RX
- U1 pad 4: /STM_VCC -> /MCU/STM_VCC
- U1 pad 6: /NRST -> /Connectors/RST
- U1 pad 7: /FUSE1_IS -> /MCU/FUSE_IS0
- U1 pad 8: /FUSE2_IS -> /MCU/FUSE_IS1
- U1 pad 9: /FUSE3_IS -> /MCU/FUSE_IS2
- U2 pad 2: +3.3V -> /Power/SW_+5V
- U2 pad 3: +5V -> +24V
- U3 pad 1: /Power/CB -> GND
- U3 pad 2: unconnected-(U3-NC-Pad2) -> /Power/VO_+3.3V
- U3 pad 3: unconnected-(U3-NC-Pad3) -> +5V
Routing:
- net +3V3: track 0.00 -> 179.1 mm, vias 0 -> 7
- net +3.3V: track 135.0 -> 0.00 mm, vias 27 -> 0
- net /MCU/SPI.NSS: track 0.00 -> 84.9 mm, vias 0 -> 6
- net GND: track 16.3 -> 86.3 mm, vias 180 -> 93
- net /SPI1_NSS: track 65.4 -> 0.00 mm, vias 6 -> 0
- net /CAN/CAN.P: track 0.00 -> 63.8 mm, vias 0 -> 2
- net /CAN/CAN.N: track 0.00 -> 62.7 mm, vias 0 -> 2
- net /MCU/SPI.SCK: track 0.00 -> 61.3 mm, vias 0 -> 6
- net /SPI1_SCK: track 60.7 -> 0.00 mm, vias 5 -> 0
- net +24V: track 0.00 -> 57.4 mm, vias 0 -> 40
- net /LHI_1: track 51.6 -> 0.00 mm, vias 2 -> 0
- net /LHI_2: track 51.5 -> 0.00 mm, vias 2 -> 0
- net /FUSE1_IS: track 48.8 -> 0.00 mm
- net /LED1: track 48.3 -> 0.00 mm, vias 2 -> 0
- net /LED2: track 48.2 -> 0.00 mm, vias 2 -> 0
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- added copper zone on F.Cu, net +24V
- added copper zone on In1.Cu, net +24V
- added copper zone on In2.Cu, net +24V
- added copper zone on B.Cu, net /CAN/CAN_GND_ISO
- added copper zone on F.Cu, net /Power/+5V_OUT
- added copper zone on F.Cu, net /Power/RPP_D
- added copper zone on F.Cu, net /Power/RPP_G
- added copper zone on F.Cu, net /Power/SW_+5V
- added copper zone on F.Cu, net /Power/VO_+3.3V
- added copper zone on B.Cu, net OUT0_0
- added copper zone on F.Cu, net OUT0_0
- added copper zone on In1.Cu, net OUT0_0
- added copper zone on In2.Cu, net OUT0_0
- added copper zone on B.Cu, net OUT0_1
- added copper zone on F.Cu, net OUT0_1
- added copper zone on In1.Cu, net OUT0_1
- added copper zone on In2.Cu, net OUT0_1
- added copper zone on B.Cu, net OUT0_2
- added copper zone on F.Cu, net OUT0_2
- added copper zone on In1.Cu, net OUT0_2
- added copper zone on In2.Cu, net OUT0_2
- added copper zone on B.Cu, net OUT0_3
- added copper zone on F.Cu, net OUT0_3
- added copper zone on In1.Cu, net OUT0_3
- added copper zone on In2.Cu, net OUT0_3
- removed copper zone on F.Cu, net +3.3V
- removed copper zone on In1.Cu, net +3.3V
- removed copper zone on B.Cu, net +BATT
- removed copper zone on F.Cu, net /Power/CB
- removed copper zone on F.Cu, net /Power/SW_L
- removed copper zone on F.Cu, net /Power/VIN_L
- removed copper zone on F.Cu, net /Power/VIN_SW_REG
- removed copper zone on F.Cu, net Net-(D10-K)
- removed copper zone on B.Cu, net OUT4_0
- removed copper zone on F.Cu, net OUT4_0
- removed copper zone on In1.Cu, net OUT4_0
- removed copper zone on In2.Cu, net OUT4_0
- removed copper zone on B.Cu, net OUT4_1
- removed copper zone on F.Cu, net OUT4_1
- removed copper zone on In1.Cu, net OUT4_1
- removed copper zone on In2.Cu, net OUT4_1
- removed copper zone on B.Cu, net OUT4_2
- removed copper zone on F.Cu, net OUT4_2
- removed copper zone on In1.Cu, net OUT4_2
- removed copper zone on In2.Cu, net OUT4_2
- removed copper zone on B.Cu, net OUT4_3
- removed copper zone on F.Cu, net OUT4_3
- removed copper zone on In1.Cu, net OUT4_3
- removed copper zone on In2.Cu, net OUT4_3
- removed copper zone on F.Cu, net VBUS
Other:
- board outline added: 85 x 58 mm
- board text removed: "Kacper Biadała"
- board text removed: "v2.0"
